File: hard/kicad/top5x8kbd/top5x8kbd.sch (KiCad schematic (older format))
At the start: 79 parts, among them J1 EXPANSION, J16 COLUMN, J17 ROW, J2 TO COMPUTER, J23 DB9_Male, J44 DB9_Male, J5 TO COMPUTER (DIRECT), SW1 1 !, SW10 0 _, SW11 Q ¡, SW12 W ~~, SW13 E é, SW14 R <, SW15 T >, SW16 Y ü, SW17 U ú, SW18 I í, SW19 O ó, SW2 2 @, SW20 P \", SW21 A á, SW22 S ;, SW23 D |, SW24 F [, SW25 G ], SW26 H ^, SW27 J -, SW28 K +, SW29 L =, SW3 3 #, SW30 ENTER ñ, SW31 SHIFT, SW32 Z :, SW33 X ¿, SW34 C ?, SW35 V /, SW36 B *, SW37 N ,, SW38 M ., SW39 ALT, SW4 4 $, SW40 SPACE, SW5 5 %, SW6 6 &, SW7 7 ', SW8 8 (, SW9 9 (, U1 74HC138, U12 74HC174, U13 74HC245, U24 74HC245, U26 74HC174, U34 74HC595, U45 74HC245, U55 74HC595, U9 74HC86

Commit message: fix cover edge cuts
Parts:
- J1: value EXPANSION -> IOx
- J2: value TO COMPUTER -> IOx
- J5: value TO COMPUTER (DIRECT) -> TO COMPUTER
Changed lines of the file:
@@
 U 1 1 635E9295
 P 8850 3750
-F 0 "J1" H 8900 4267 50  0000 C CNN
-F 1 "EXPANSION" H 9000 4150 50  0000 C CNN
+F 0 "J1" H 8900 4250 50  0000 C CNN
+F 1 "IOx" H 8900 4150 50  0000 C CNN
 F 2 "Connector_IDC:IDC-Header_2x08_P2.54mm_Vertical" H 8850 3750 50  0001 C CNN
 F 3 "~" H 8850 3750 50  0001 C CNN
@@
 P 8850 2550
 F 0 "J2" H 8900 3067 50  0000 C CNN
-F 1 "TO COMPUTER" H 9050 2950 50  0000 C CNN
+F 1 "IOx" H 8900 2950 50  0000 C CNN
 F 2 "Connector_IDC:IDC-Header_2x08_P2.54mm_Vertical" H 8850 2550 50  0001 C CNN
 F 3 "~" H 8850 2550 50  0001 C CNN
@@
 P 8850 1350
 F 0 "J5" H 8900 1867 50  0000 C CNN
-F 1 "TO COMPUTER (DIRECT)" H 9250 1750 50  0000 C CNN
+F 1 "TO COMPUTER" H 9000 1750 50  0000 C CNN
 F 2 "Connector_PinSocket_2.54mm:PinSocket_2x08_P2.54mm_Vertical" H 8850 1350 50  0001 C CNN
 F 3 "~" H 8850 1350 50  0001 C CNN

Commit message: improve silkmask
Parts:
- J23: value DB9_Male -> MD/VCS1
- J44: value DB9_Male -> MD/VCS2
- RN11: value 22K -> 10K
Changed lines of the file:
@@
 P 7800 1350
 F 0 "J23" H 7980 1396 50  0000 L CNN
-F 1 "DB9_Male" H 7980 1305 50  0000 L CNN
+F 1 "MD/VCS1" H 7980 1305 50  0000 L CNN
 F 2 "Connector_Dsub:DSUB-9_Male_Horizontal_P2.77x2.84mm_EdgePinOffset4.94mm_Housed_MountingHolesOffset7.48mm" H 7800 1350 50  0001 C CNN
 F 3 " ~" H 7800 1350 50  0001 C CNN
@@
 P 7800 2450
 F 0 "J44" H 7980 2496 50  0000 L CNN
-F 1 "DB9_Male" H 7980 2405 50  0000 L CNN
+F 1 "MD/VCS2" H 7980 2405 50  0000 L CNN
 F 2 "Connector_Dsub:DSUB-9_Male_Horizontal_P2.77x2.84mm_EdgePinOffset4.94mm_Housed_MountingHolesOffset7.48mm" H 7800 2450 50  0001 C CNN
 F 3 " ~" H 7800 2450 50  0001 C CNN
@@
 P 6200 1450
 F 0 "RN11" V 5583 1450 50  0000 C CNN
-F 1 "22K" V 5674 1450 50  0000 C CNN
+F 1 "10K" V 5674 1450 50  0000 C CNN
 F 2 "Resistor_THT:R_Array_SIP9" V 6675 1450 50  0001 C CNN
 F 3 "http://www.vishay.com/docs/31509/csc.pdf" H 6200 1450 50  0001 C CNN

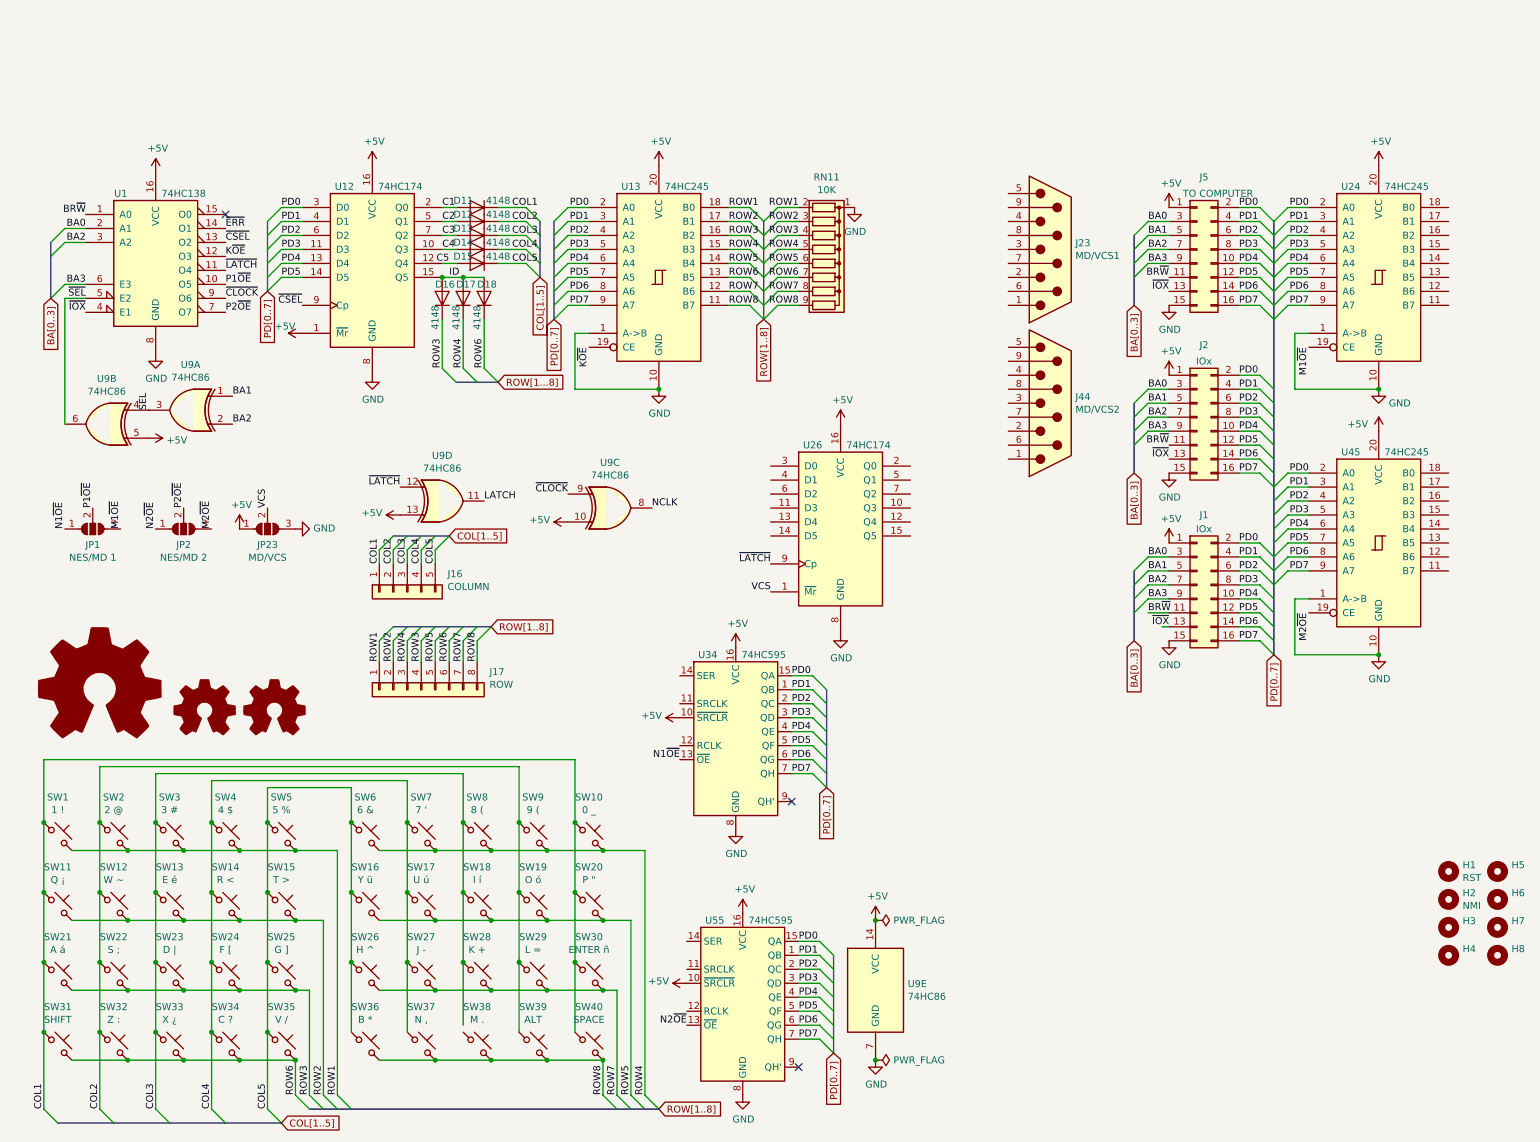
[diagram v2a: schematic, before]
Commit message: complete 5x8 schematic
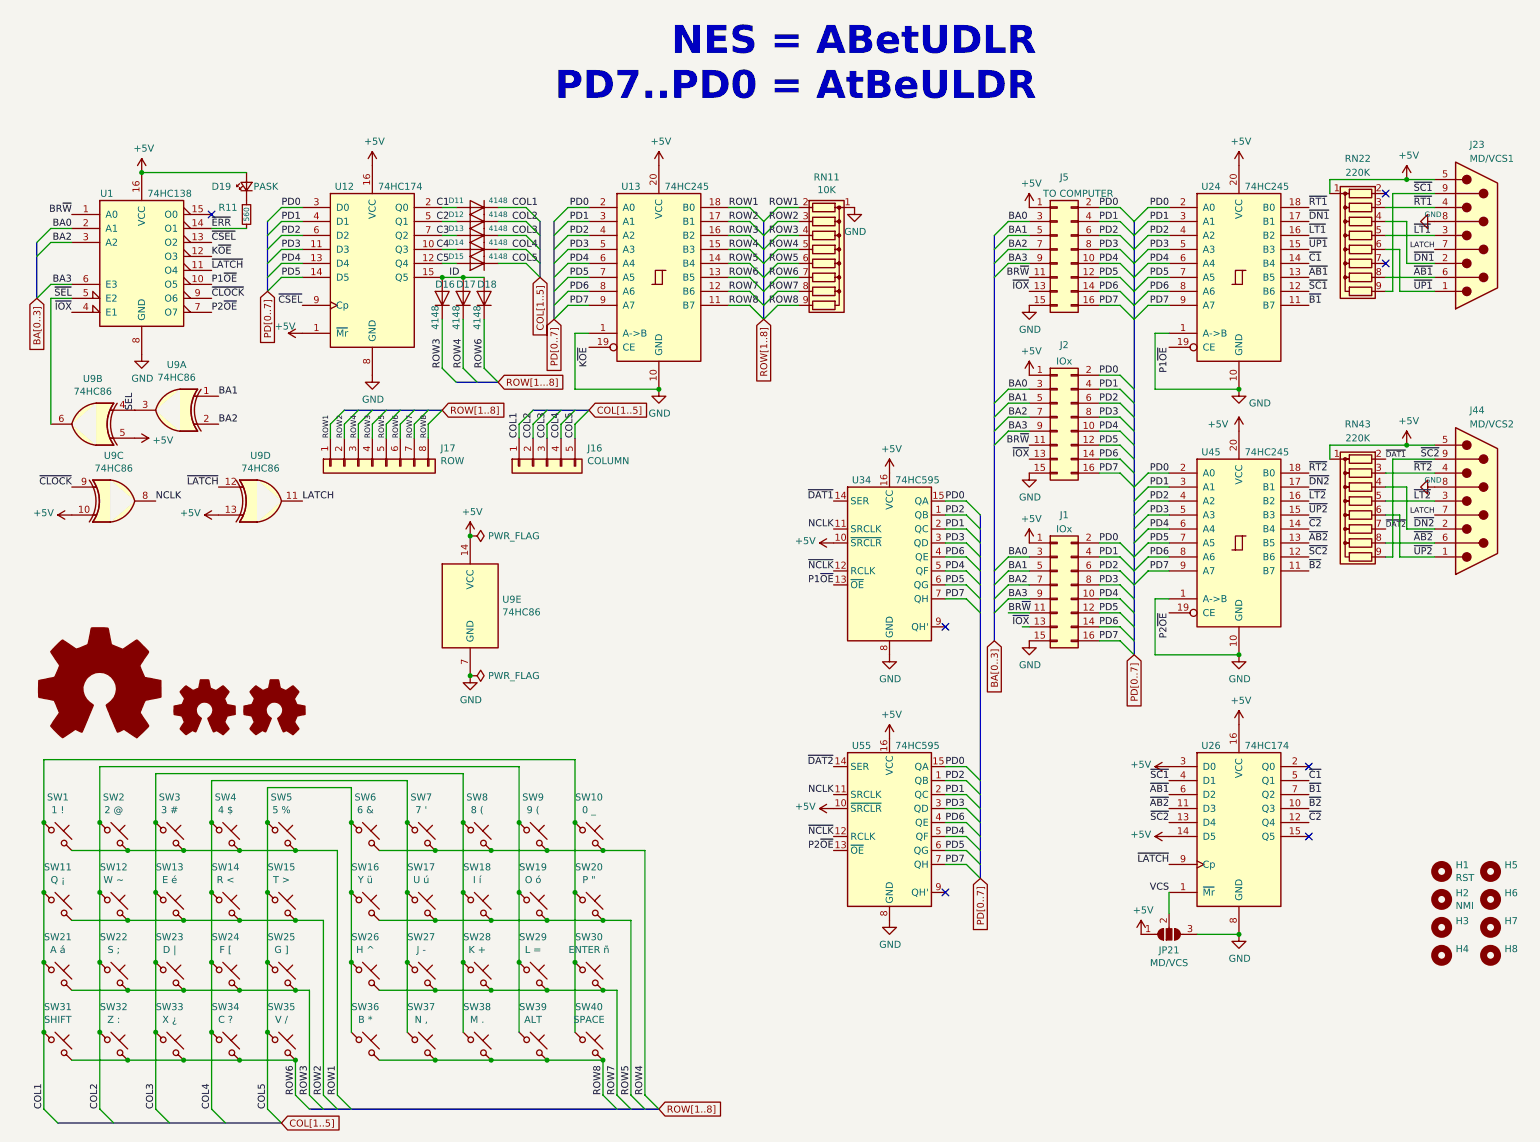
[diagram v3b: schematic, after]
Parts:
- removed JP1: NES/MD 1, Jumper:SolderJumper-3_P1.3mm_Open_RoundedPad1.0x1.5mm, symbol Jumper:SolderJumper_3_Open
- removed JP2: NES/MD 2, Jumper:SolderJumper-3_P1.3mm_Open_RoundedPad1.0x1.5mm, symbol Jumper:SolderJumper_3_Open
- added D19: PASK, LED_THT:LED_D3.0mm, symbol Device:LED_Small
- added R11: 560, Resistor_THT:R_Axial_DIN0207_L6.3mm_D2.5mm_P10.16mm_Horizontal, symbol Device:R_Small
- added RN22, RN43: 220K, Resistor_THT:R_Array_SIP9, symbol Device:R_Network08
- U1, U12, U26, U34, U55: footprint Package_DIP:DIP-16_W7.62mm -> Package_DIP:DIP-16_W7.62mm_Socket
- U13, U24, U45: footprint Package_DIP:DIP-20_W7.62mm -> Package_DIP:DIP-20_W7.62mm_Socket
- U9: footprint Package_DIP:DIP-14_W7.62mm -> Package_DIP:DIP-14_W7.62mm_Socket
- renumbered JP23 to JP21
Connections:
- net M1~OE is gone; now on net P1~OE: U24.19 (CE)
- net M2~OE is gone; now on net P2~OE: U45.19 (CE)
- net N1~OE is gone; now on net P1~OE: U34.13 (~OE)
- net N2~OE is gone; now on net P2~OE: U55.13 (~OE)
- net +5V: now also J23.5, J44.5, U26.14 (D5), U26.3 (D0), D19.2 (A), RN22.1 (common), RN43.1 (common)
- net COL3: now also SW38.1
- net GND: now also J23.8, J44.8
- net LATCH: now also J23.7, J44.7
- net NCLK: now also U34.11 (SRCLK), U55.11 (SRCLK)
- net PD1: now also U34.2 (QC), U55.2 (QC); no longer U34.1 (QB), U55.1 (QB)
- net PD2: now also U34.1 (QB), U55.1 (QB); no longer U34.2 (QC), U55.2 (QC)
- net PD4: now also U34.5 (QF), U55.5 (QF); no longer U34.4 (QE), U55.4 (QE)
- net PD5: now also U34.6 (QG), U55.6 (QG); no longer U34.5 (QF), U55.5 (QF)
- net PD6: now also U34.4 (QE), U55.4 (QE); no longer U34.6 (QG), U55.6 (QG)
- net ~ERR: now also R11.2
- net ~UP1: now reaches J23.1
- net ~UP1: now also U24.15 (B3), RN22.6 (R5)
- net ~DN1: now reaches J23.2
- net ~DN1: now also U24.17 (B1), RN22.4 (R3)
- net ~LT1: now reaches J23.3
- net ~LT1: now also U24.16 (B2), RN22.5 (R4)
- net ~RT1: now reaches J23.4
- net ~RT1: now also U24.18 (B0), RN22.3 (R2)
- net ~AB1: now reaches J23.6
- net ~AB1: now also U24.13 (B5), U26.6 (D2), RN22.8 (R7)
- net ~SC1: now reaches J23.9
- net ~SC1: now also U24.12 (B6), U26.4 (D1), RN22.9 (R8)
- net ~UP2: now reaches J44.1
- net ~UP2: now also U45.15 (B3), RN43.6 (R5)
- net ~DN2: now reaches J44.2
- net ~DN2: now also U45.17 (B1), RN43.4 (R3)
- net ~LT2: now reaches J44.3
- net ~LT2: now also U45.16 (B2), RN43.5 (R4)
- net ~RT2: now reaches J44.4
- net ~RT2: now also U45.18 (B0), RN43.3 (R2)
- net ~AB2: now reaches J44.6
- net ~AB2: now also U26.11 (D3), U45.13 (B5), RN43.8 (R7)
- net ~SC2: now reaches J44.9
- net ~SC2: now also U26.13 (D4), U45.12 (B6), RN43.9 (R8)
- net ~B2: now reaches U26.10 (Q3)
- net ~B2: now also U45.11 (B7)
- net ~C2: now reaches U26.12 (Q4)
- net ~C2: now also U45.14 (B4)
- net ~C1: now reaches U26.5 (Q1)
- net ~C1: now also U24.14 (B4)
- net ~B1: now reaches U26.7 (Q2)
- net ~B1: now also U24.11 (B7)
- net ~NCLK: now reaches U55.12 (RCLK)
- net ~NCLK: now also U34.12 (RCLK)
- net ~DAT2: now reaches U55.14 (SER)
- net ~DAT2: now also RN43.7 (R6)
- net ~DAT1: now reaches U34.14 (SER)
- net ~DAT1: now also RN43.2 (R1)
- new net: D19.1 (K), R11.1
- no-connect marks 3 -> 7
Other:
- note added: "NES = ABetUDLR\nPD7..PD0 = AtBeULDR"
- moved on the sheet: H1, H2, H3, H4, H5, H6, H7, H8, J1, J16, J17, J2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

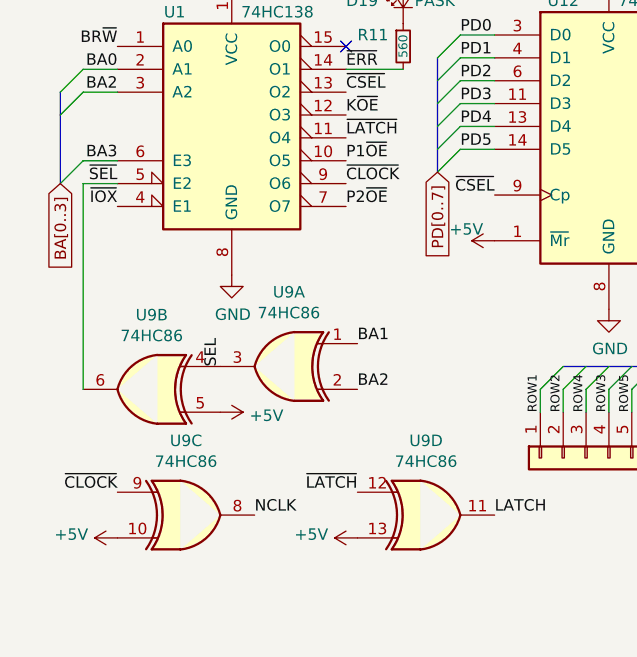
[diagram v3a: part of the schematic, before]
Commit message: fix silkscreen, missing NES conn schematic
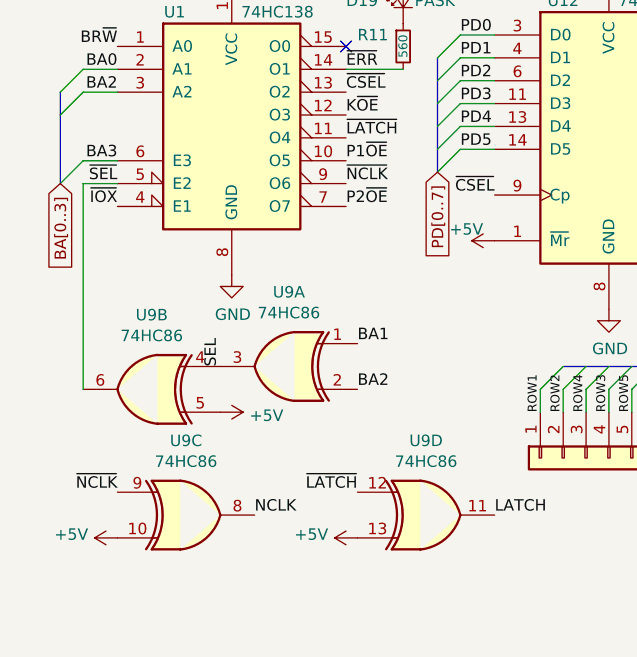
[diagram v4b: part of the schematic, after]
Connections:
- net ~CLOCK is gone; now on net ~NCLK: U1.9 (O6), U9.9
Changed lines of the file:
@@
 ~LATCH
 Text Label 1800 1700 0    50   ~ 0
-~CLOCK
+~NCLK
 NoConn ~ 1800 1100
 Text Label 1800 1300 0    50   ~ 0
@@
 $EndComp
 Text Label 800  3050 2    50   ~ 0
-~CLOCK
+~NCLK
 Text Label 1400 3150 0    50   ~ 0
 NCLK
@@
 Text Label 9650 5450 0    50   ~ 0
 ~C2
+Text Label 6250 3350 2    50   ~ 0
+NCLK
+Text Label 6250 3650 2    50   ~ 0
+~NCLK
+Text Label 6250 5250 2    50   ~ 0
+NCLK
+Text Label 6250 5550 2    50   ~ 0
+~NCLK
 Wire Bus Line
 	3550 2300 3850 2300
@@
 Wire Bus Line
 	8400 1150 8400 4250
-Text Label 6250 3350 2    50   ~ 0
-NCLK
-Text Label 6250 3650 2    50   ~ 0
-~NCLK
-Text Label 6250 5250 2    50   ~ 0
-NCLK
-Text Label 6250 5550 2    50   ~ 0
-~NCLK
 $EndSCHEMATC

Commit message: makeshift NES connector placement
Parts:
- added J33: NES 1, Connector_PinHeader_2.54mm:PinHeader_2x04_P2.54mm_Horizontal, symbol Connector_Generic:Conn_2Rows-07Pins
- added J54: NES 2, Connector_PinHeader_2.54mm:PinHeader_2x04_P2.54mm_Horizontal, symbol Connector_Generic:Conn_2Rows-07Pins
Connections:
- net +5V: now also J33.6 (Pin_6), J54.6 (Pin_6)
- net GND: now also J33.7 (Pin_7), J54.7 (Pin_7)
- net LATCH: now also J33.3 (Pin_3), J54.3 (Pin_3)
- net NCLK: now also J33.5 (Pin_5), J54.5 (Pin_5)
- net ~DAT1: now also J33.1 (Pin_1)
- net ~DAT2: now also J54.1 (Pin_1)
- no-connect marks 7 -> 11
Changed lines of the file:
@@
 Text Label 6250 5550 2    50   ~ 0
 ~NCLK
+$Comp
+L Connector_Generic:Conn_2Rows-07Pins J33
+U 1 1 63729BC7
+P 5600 3050
+F 0 "J33" H 5650 2625 50  0000 C CNN
+F 1 "NES 1" H 5650 2716 50  0000 C CNN
+F 2 "Connector_PinHeader_2.54mm:PinHeader_2x04_P2.54mm_Horizontal" H 5600 3050 50  0001 C CNN
+F 3 "~" H 5600 3050 50  0001 C CNN
+	1    5600 3050
+	-1   0    0    1
+$EndComp
+Wire Wire Line
+	5800 3150 6250 3150
+Wire Wire Line
+	5800 2950 5850 2950
+Wire Wire Line
+	5850 2950 5850 3350
+Wire Wire Line
+	5850 3350 6250 3350
+Wire Wire Line
+	5800 3050 5900 3050
+Text Label 5900 3050 0    50   ~ 0
+LATCH
+$Comp
+L power:GND #PWR0139
+U 1 1 637AE05E
+P 5800 2850
+F 0 "#PWR0139" H 5800 2600 50  0001 C CNN
+F 1 "GND" V 5805 2722 50  0000 R CNN
+F 2 "" H 5800 2850 50  0001 C CNN
+F 3 "" H 5800 2850 50  0001 C CNN
+	1    5800 2850
+	0    -1   -1   0
+$EndComp
+NoConn ~ 5300 3050
+NoConn ~ 5300 3150
+$Comp
+L power:+5V #PWR0140
+U 1 1 63820300
+P 5300 2950
+F 0 "#PWR0140" H 5300 2800 50  0001 C CNN
+F 1 "+5V" H 5315 3123 50  0000 C CNN
+F 2 "" H 5300 2950 50  0001 C CNN
+F 3 "" H 5300 2950 50  0001 C CNN
+	1    5300 2950
+	1    0    0    -1
+$EndComp
+$Comp
+L Connector_Generic:Conn_2Rows-07Pins J54
+U 1 1 63820413
+P 5600 4950
+F 0 "J54" H 5650 4525 50  0000 C CNN
+F 1 "NES 2" H 5650 4616 50  0000 C CNN
+F 2 "Connector_PinHeader_2.54mm:PinHeader_2x04_P2.54mm_Horizontal" H 5600 4950 50  0001 C CNN
+F 3 "~" H 5600 4950 50  0001 C CNN
+	1    5600 4950
+	-1   0    0    1
+$EndComp
+Wire Wire Line
+	5800 5050 6250 5050
+Wire Wire Line
+	5800 4850 5850 4850
+Wire Wire Line
+	5850 4850 5850 5250
+Wire Wire Line
+	5850 5250 6250 5250
+Wire Wire Line
+	5800 4950 5900 4950
+Text Label 5900 4950 0    50   ~ 0
+LATCH
+$Comp
+L power:GND #PWR0141
+U 1 1 63820423
+P 5800 4750
+F 0 "#PWR0141" H 5800 4500 50  0001 C CNN
+F 1 "GND" V 5805 4622 50  0000 R CNN
+F 2 "" H 5800 4750 50  0001 C CNN
+F 3 "" H 5800 4750 50  0001 C CNN
+	1    5800 4750
+	0    -1   -1   0
+$EndComp
+NoConn ~ 5300 4950
+NoConn ~ 5300 5050
+$Comp
+L power:+5V #PWR0142
+U 1 1 6382042F
+P 5300 4850
+F 0 "#PWR0142" H 5300 4700 50  0001 C CNN
+F 1 "+5V" H 5315 5023 50  0000 C CNN
+F 2 "" H 5300 4850 50  0001 C CNN
+F 3 "" H 5300 4850 50  0001 C CNN
+	1    5300 4850
+	1    0    0    -1
+$EndComp
 Wire Bus Line
 	3550 2300 3850 2300

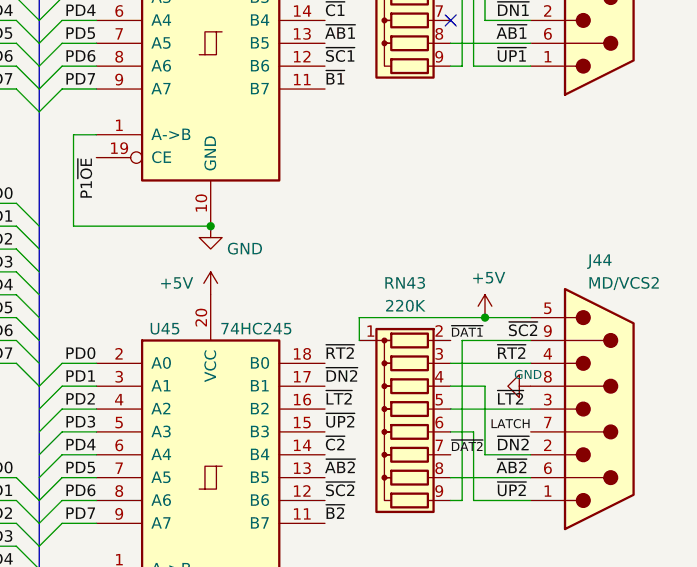
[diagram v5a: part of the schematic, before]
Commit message: NES footprint on elongated cover keyboard
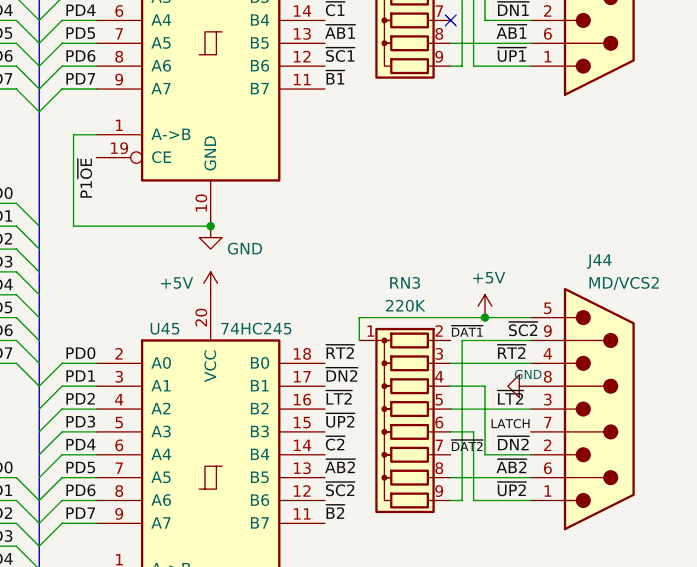
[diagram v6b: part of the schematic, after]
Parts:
- J33, J54: footprint Connector_PinHeader_2.54mm:PinHeader_2x04_P2.54mm_Horizontal -> durango:NES gamepad
- renumbered RN43 to RN3
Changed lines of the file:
@@
 $EndComp
 $Comp
-L Device:R_Network08 RN43
+L Device:R_Network08 RN3
 U 1 1 63FD1BA2
 P 10000 3250
-F 0 "RN43" V 9350 3250 50  0000 C CNN
+F 0 "RN3" V 9350 3250 50  0000 C CNN
 F 1 "220K" V 9450 3250 50  0000 C CNN
 F 2 "Resistor_THT:R_Array_SIP9" V 10475 3250 50  0001 C CNN
@@
 F 0 "J33" H 5650 2625 50  0000 C CNN
 F 1 "NES 1" H 5650 2716 50  0000 C CNN
-F 2 "Connector_PinHeader_2.54mm:PinHeader_2x04_P2.54mm_Horizontal" H 5600 3050 50  0001 C CNN
+F 2 "durango:NES gamepad" H 5600 3050 50  0001 C CNN
 F 3 "~" H 5600 3050 50  0001 C CNN
 	1    5600 3050
@@
 F 0 "J54" H 5650 4525 50  0000 C CNN
 F 1 "NES 2" H 5650 4616 50  0000 C CNN
-F 2 "Connector_PinHeader_2.54mm:PinHeader_2x04_P2.54mm_Horizontal" H 5600 4950 50  0001 C CNN
+F 2 "durango:NES gamepad" H 5600 4950 50  0001 C CNN
 F 3 "~" H 5600 4950 50  0001 C CNN
 	1    5600 4950
